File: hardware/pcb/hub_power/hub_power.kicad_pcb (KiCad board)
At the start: 2 copper layers, 44 x 81.2 mm, 58 parts, among them J1 XIAO D0-D6, J10 BAT (JST-PH), J13 USB-C, J14 XIAO PWR, J2 OLED, J4 SPK IN, J5 SPK OUT, J6 REED+BTN2, K31 G6S-2F DC5, Q1 MMUN2133LT1G, Q31 SS8050, SW1 MST-12D18G3, U1 TPS61090RSAR, U2 MCP73871-2CCI/ML, U3 INA226AIDGSR, U4 AS5600-ASOM

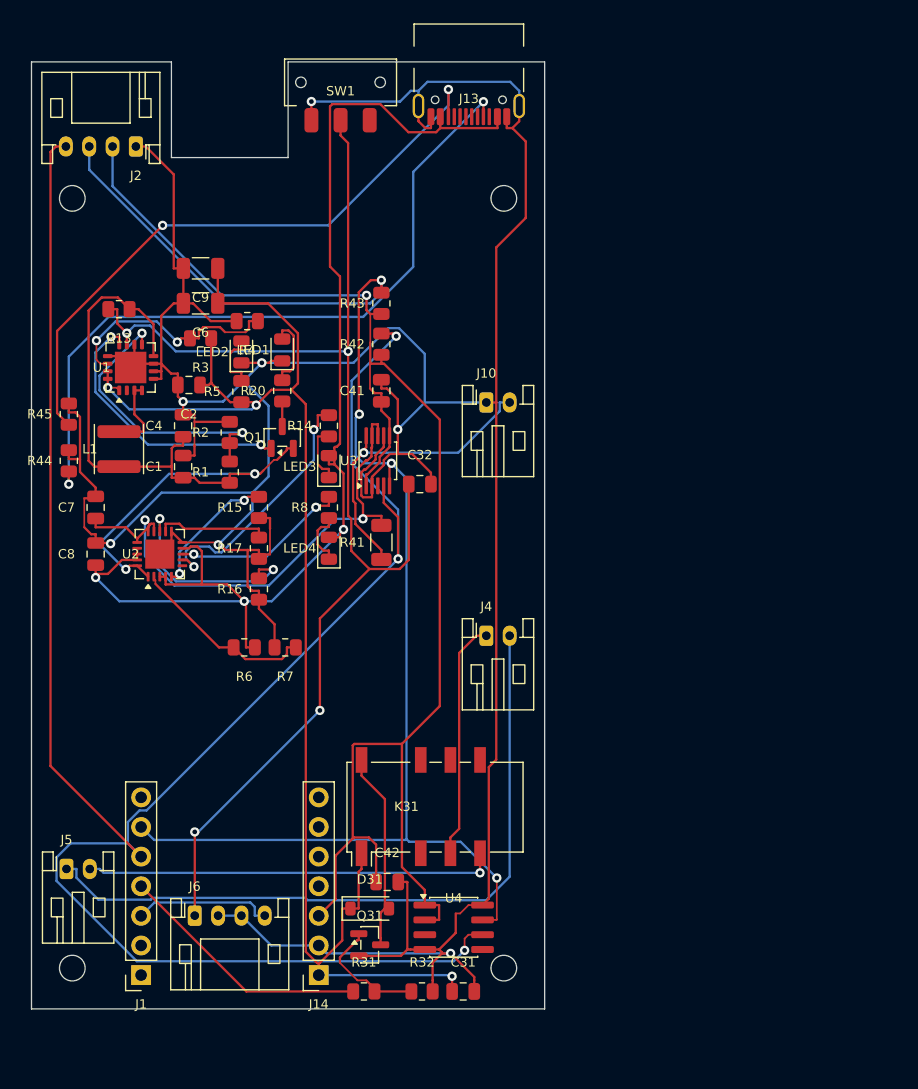
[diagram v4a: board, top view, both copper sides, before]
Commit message: リレーを立入禁止の円から出して AS5600 から離す（機構担当の B1）
- K31 の芯を Y 17.35 → 18.85。立入禁止 φ10.2（芯 36.2, 7）への食い込み 0.10 が
  余裕 1.40 になり、枠は Y 13.50〜24.20（電池の影の縁 25 まで残り 0.8）
- ついでに AS5600 の芯から 10.5 → 11.95mm 離した（リレーのコイルの磁気の件）
- B2（ブラケットの彫り込み）と B3（SOIC-8 の向き）は板側の変更なし。
  B3 は機構側のモデルが 90 度回っていたので、ランドは直さない

配線 638 本・未配線 0・DRC エラー 0・プラグの通り道 5 口すべて空き・
check_pcb は下限 0.15mm に対していちばん近いのが 0.151mm
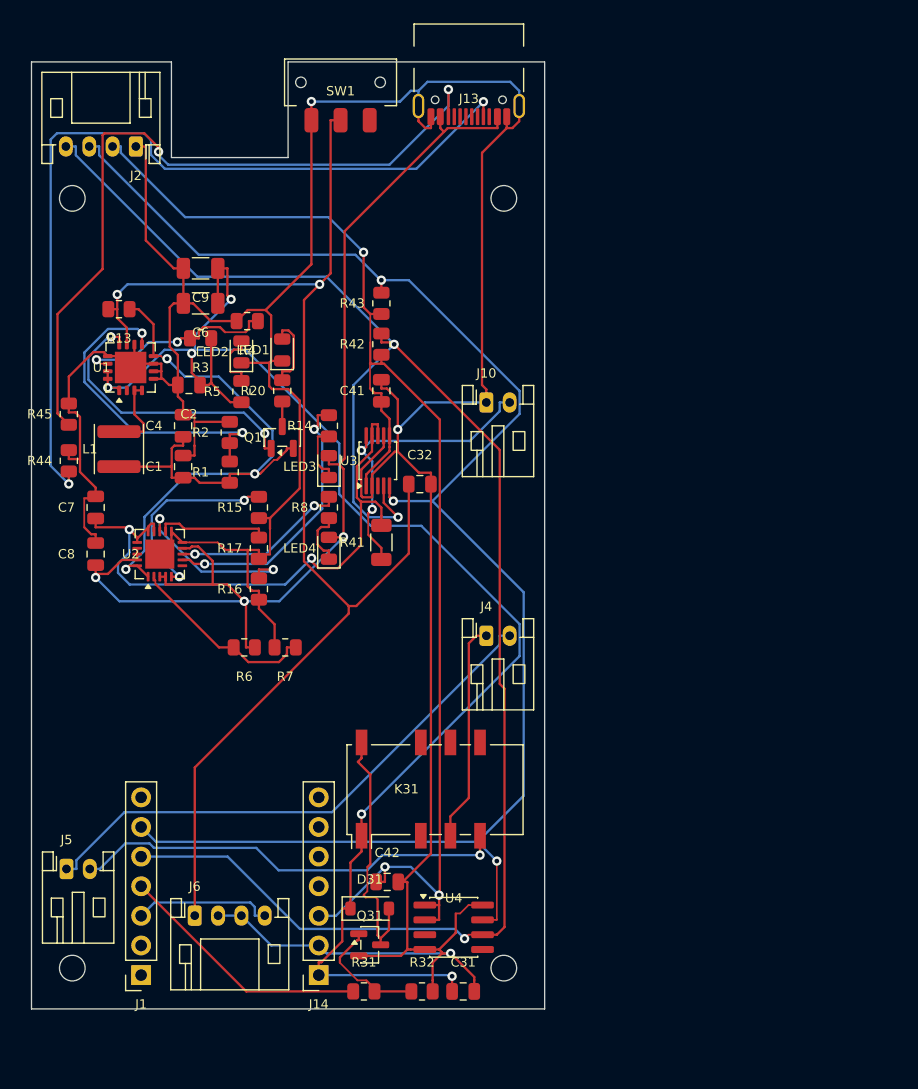
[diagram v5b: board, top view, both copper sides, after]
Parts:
- moved K31 1.50 mm to (94.7, 102.3)
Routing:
- net SDA: track 181.1 -> 148.4 mm
- net GND: track 339.6 -> 318.1 mm, vias 7 -> 3
- net SPKM: track 61.2 -> 47.2 mm
- net V33: track 130.2 -> 117.9 mm, vias 1 -> 3
- net CC1: track 62.7 -> 74.3 mm
- net SCL: track 126.1 -> 136.5 mm, vias 4 -> 3
- net CC2: track 53.7 -> 63.9 mm
- net VBUS: track 106.5 -> 97.6 mm
- net VSYS: track 67.8 -> 62.3 mm, vias 2 -> 3
- net THERM: track 11.4 -> 16.8 mm
- net VLIPO: track 46.6 -> 51.7 mm
- net COL: track 17.2 -> 22.1 mm
- net V5: track 121.0 -> 125.9 mm, vias 3 -> 5
- net LBI: track 24.6 -> 28.3 mm
- net EN: track 110.1 -> 113.1 mm, vias 4 -> 2
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
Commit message: 両面に GND のベタを敷いて板を通す・ナットと通り道の検査を足す
筐体側から「取付穴のナット（二面幅 4.0・背 1.6）の下に部品が寄っていないか」と聞かれて
数えたら 3 つ当たっていた。直す過程で自動配線が詰まったので、構造から直した。

- 🔴 ナットの検査を足した。MOUNT_KEEP は銅の話で部品の背の話ではない。
  J5 と C31 を逃がした。U4（AS5600）だけは磁石の真下から動かせないので残っている
- 🔴 プラグの通り道も「押し出す所」に入れた。入れないと他の部品が後から流れ込む
  （電源ブロックを広げたら J2 の通り道に U1 と R13 が入った）
- 🔴 CC の引き下げ 2 本を USB-C の足元へ。旧電源板の並びを写したままで 40mm 離れ、
  CC2 が 1 本つながっていなかった
- 電源ブロックを電池の影いっぱいに広げた（旧 40 × 32 の詰め方のままだった）
- 🔴 表と裏に GND のベタを敷き、島を縫うビアを 173 個打つ route.py の stitch() を足した。
  ⚠ GND は自動配線にも渡す。ベタ任せにすると U3 の細ピッチの GND にベタが入らない
- パッドはベタ直結（thermal relief を使わない）。足付きだけ thermal にすると PH や
  USB-C のシェルの幅 1.0mm のパッドで spoke が 1 本しか立たず starved_thermal が残る。
  ⚠ 代償として手はんだの GND 7 点に熱が逃げる
- drc に --refill-zones を足した（--save-board は付けない。板を KiCad に書き直させると
  次の merge() が読めなくなる）

結果: 配線 628 本 ＋ 縫うビア 173 個・**未配線 0・DRC エラー 0**・
check_sch 0 件・check_pcb は下限 0.15mm に対していちばん近いのが 0.152mm・
プラグの通り道 5 口すべて空き・パッドの位置の検算 4 点一致。

ついでに POWER.md のリードの沈み代を 0.70 → 0.58 に直した（0.30 は立った壁の値で、
平たい肉の実績は 0.42）。数は磁石の半径が決まってから数え直す。
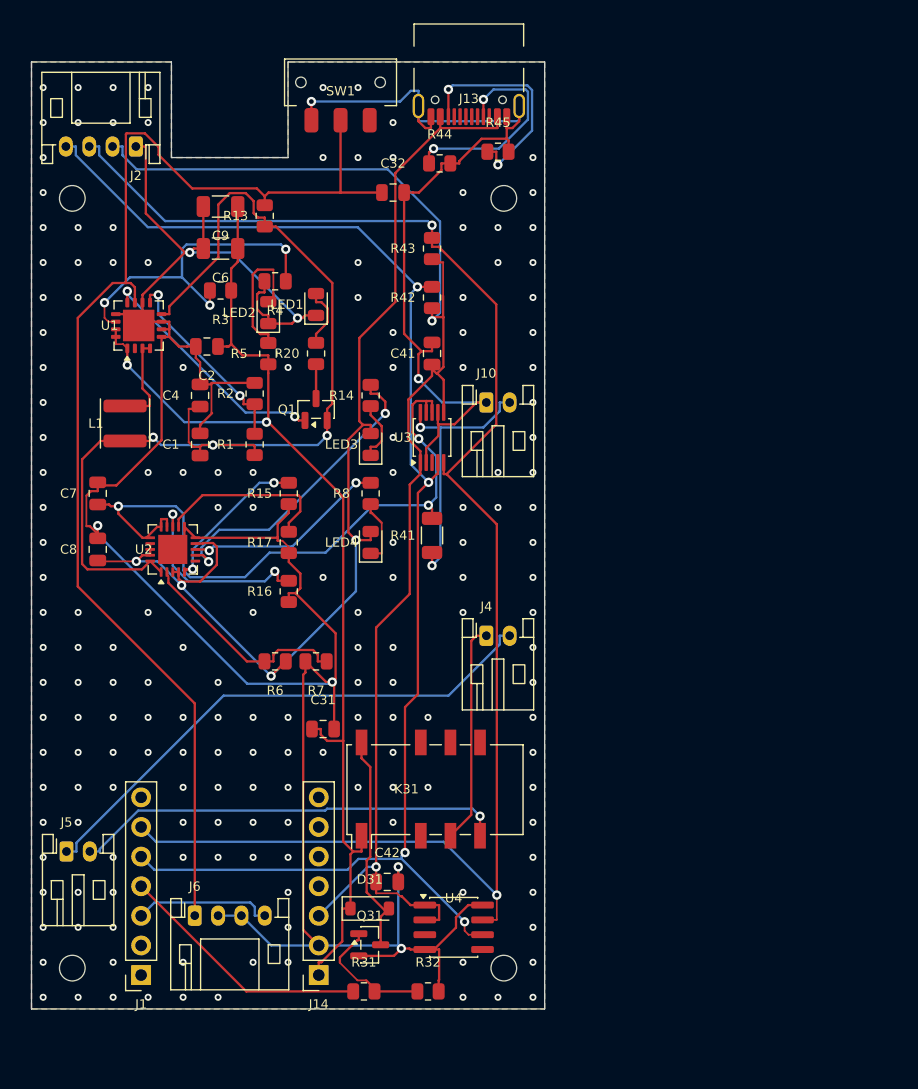
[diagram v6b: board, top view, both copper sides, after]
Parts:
- moved R45 43.1 mm to (100.0, 47.7), turned to 0 degrees
- moved R44 40.8 mm to (95.0, 48.7), turned to 0 degrees
- moved C31 25.5 mm to (85.0, 97.2)
- moved C32 25.1 mm to (91.0, 51.2)
- moved R13 14.8 mm to (80.0, 53.2), turned to 90 degrees
- moved R43 6.40 mm to (94.3, 56.0)
- moved R42 5.91 mm to (94.3, 60.2)
- moved C9 5.57 mm to (76.2, 52.4)
- moved C41 5.40 mm to (94.3, 65.0)
- moved U3 5.06 mm to (94.3, 72.2)
- moved C6 5.00 mm to (76.2, 56.0)
- moved LED1 4.86 mm to (84.4, 60.8)
- moved R3 4.44 mm to (76.2, 59.6)
- moved R14 4.42 mm to (89.1, 68.6)
- moved R41 4.39 mm to (94.3, 80.6)
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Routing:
- net CC1: track 74.3 -> 18.7 mm
- net CC2: track 63.9 -> 19.4 mm
- net V5: track 125.9 -> 98.1 mm, vias 5 -> 2
- net VSYS: track 62.3 -> 89.9 mm
- net SDA: track 148.4 -> 123.0 mm, vias 3 -> 4
- net GND: track 318.1 -> 300.4 mm, vias 3 -> 181
- net FB: track 17.4 -> 29.0 mm, vias 2 -> 3
- net LBI: track 28.3 -> 17.3 mm
- net VLIPO: track 51.7 -> 58.8 mm, vias 2 -> 3
- net N_LED2: track 5.11 -> 11.7 mm
- net PROG3: track 9.60 -> 15.4 mm
- net EN: track 113.1 -> 107.5 mm, vias 2 -> 0
- net LBO: track 24.8 -> 21.0 mm
- net THERM: track 16.8 -> 13.1 mm
- net STAT2: track 23.5 -> 26.7 mm
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- added copper zone on B.Cu, net GND
- added copper zone on F.Cu, net GND

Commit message: 背面の柱 6 本の抜きを入れて引き直す（⚠ 未配線が 1 本残っている）
🔒 調停役 2026-09-13「解放します。1 回で入れてください」。抜きは確定値で入れた。

- 外形に丸い抜きを 6 つ（OLED × 4 φ6.5・ReSpeaker × 2 φ4.0・合計 157.9mm²）。
  まわり 0.5 に銅を置かせない（0.3 だと KiCad の copper_edge_clearance が出た）
- 抜きを relax の押し出す所と DSN の keepout と縫うビアの除外に入れた
- 🔴 **OLED の柱 (3.30, 71.80) が上の縁の唯一の 4 ピンの枠を奪った。**総当たりで探したら
  PH 4 ピンが入るのは谷と右の帯（口を −X へ）の 2 つだけで、谷には J6 が居る。
  ⇒ OLED の口を右の帯（X 35〜43.6・Y 43.5〜54.5）へ回した。口は板の内側 −X を向く。
  線は伸びるが、谷へ入れた場合の 65mm より短い（芯どうし約 35mm）
- その通り道が電池の影を横切るので、電源ブロックの並びを組み替えた。
  pwr() の倍率を X 1.13 / Y 1.32 にし、通り道に落ちる 8 つ（U3・C41・R42・R8・LED3・
  R14・LED4・Q1）は手で左へ置いた
- ミュートリレーの駆動を K31 の左上の帯（Y 20〜25）へ。柱の抜きで J14 と柱のあいだが
  2.88mm しか残らなくなったため
- 🔒 取付穴 (40.5, 3.5) の U4 はナットの検査から除外した。ナットはブラケットの足の上
  （BRK_FT 2.15 ⇒ 底 6.75）で U4 の天面 6.45 を 0.30 の隙間で宙で跨ぐ

検査: 取付穴 4 か所ともナットの下は空き・プラグの通り道 5 口すべて空き・
パッドの位置の検算 4 点一致・部品の重なり 0・板からのはみ出し 0・
check_sch 0 件・check_pcb は下限 0.15mm に対していちばん近いのが 0.152mm。

🔴 **未配線が 1 本残っている**: J13（USB-C）の VBUS のパッド A4。VBUS は 4 パッドあり
3 本までつながって 1 本が届かない。原因は OLED の柱 (40.70, 71.80) の抜きが USB-C の
足元を塞いでいること。倍率を 1.08〜1.20 で振って 1.13 が最小（他は 2〜4 本）。
CC の抵抗を動かすと今度は J4 の通り道が塞がる。**次はここを解く。**
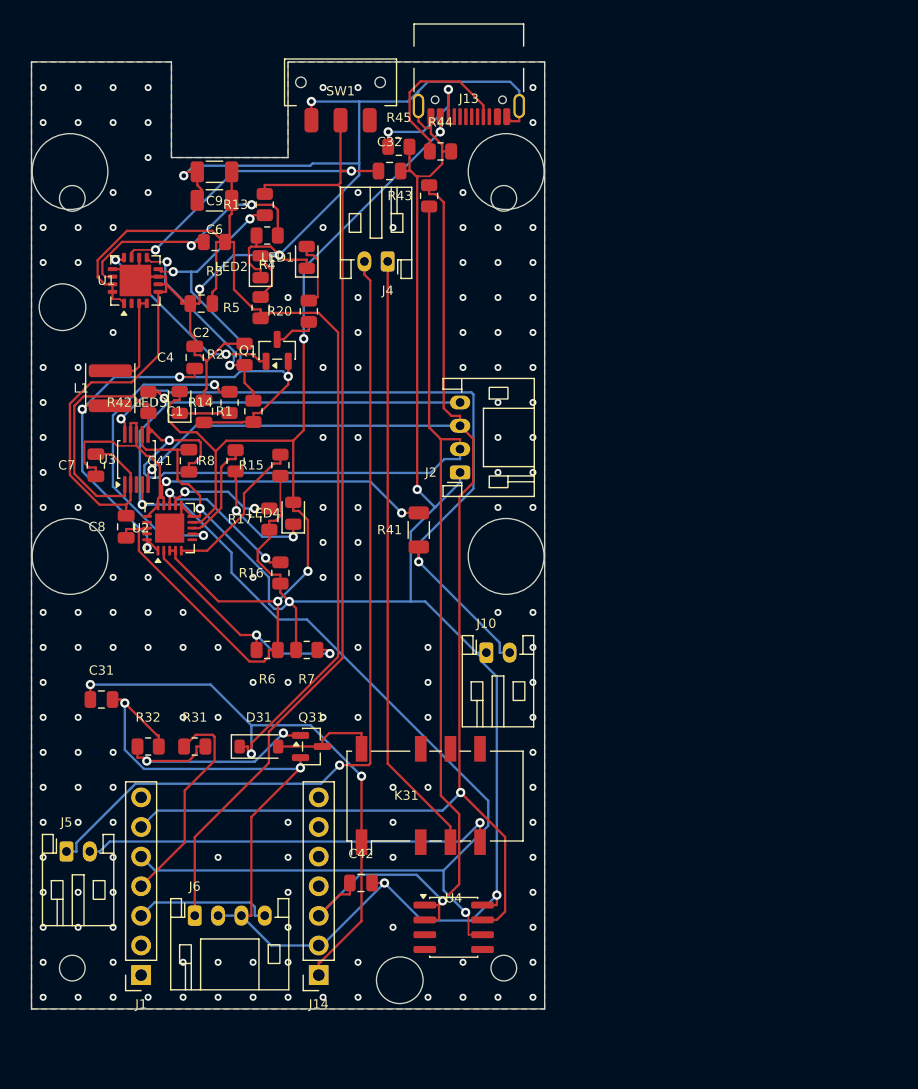
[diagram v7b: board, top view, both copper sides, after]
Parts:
- removed the C31 at (85.0, 97.2)
- removed the J10 at (99.0, 69.2)
- removed the J2 at (69.0, 47.2)
- added J4: SPK IN, Connector_JST:JST_PH_S2B-PH-K_1x02_P2.00mm_Horizontal, F.Cu at (90.5, 57.1)
- added J6: REED+BTN2, Connector_JST:JST_PH_S4B-PH-K_1x04_P2.00mm_Horizontal, F.Cu at (74.0, 113.2)
- added Q31: SS8050, Package_TO_SOT_SMD:SOT-23, F.Cu at (84.0, 98.7)
- C31: renamed from R31; value 1k -> 0.1uF; footprint Resistor_SMD:R_0805_2012Metric -> Capacitor_SMD:C_0805_2012Metric
- J10: renamed from J6; value REED+BTN2 -> BAT (JST-PH); footprint Connector_JST:JST_PH_S4B-PH-K_1x04_P2.00mm_Horizontal -> Connector_JST:JST_PH_S2B-PH-K_1x02_P2.00mm_Horizontal
- J2: renamed from J4; value SPK IN -> OLED; footprint Connector_JST:JST_PH_S2B-PH-K_1x02_P2.00mm_Horizontal -> Connector_JST:JST_PH_S4B-PH-K_1x04_P2.00mm_Horizontal
- R31: renamed from Q31; value SS8050 -> 1k; footprint Package_TO_SOT_SMD:SOT-23 -> Resistor_SMD:R_0805_2012Metric
- moved ? 75.7 mm to (63.5, 117.7)
- moved ? 75.7 mm to (100.5, 51.7)
- moved J10 33.7 mm to (99.0, 90.7)
- moved C31 33.7 mm to (66.0, 94.7)
- moved R32 31.9 mm to (70.0, 98.7)
- moved R42 25.9 mm to (70.0, 69.2)
- moved U3 25.4 mm to (69.0, 74.1)
- moved C41 22.8 mm to (73.5, 74.2)
- moved R31 22.7 mm to (74.0, 98.7)
- moved D31 16.8 mm to (79.5, 98.7)
- moved LED3 16.8 mm to (72.7, 69.2)
- moved J2 14.2 mm to (96.8, 75.2), turned to 90 degrees
- moved R14 12.1 mm to (77.0, 69.2)
- moved R8 11.9 mm to (77.5, 74.2)
- moved R45 8.51 mm to (91.5, 47.3)
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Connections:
- C31 pad 1: IN -> V5
- C31 pad 2: BASE -> GND
- J10 pad 1: EN -> GND
- J10 pad 2: GND -> BATP
- J2 pad 1: SPKP -> GND
- J2 pad 2: SPKM -> V33
- R31 pad 1: BASE -> IN
- R31 pad 2: GND -> BASE
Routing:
- net GND: track 300.4 -> 359.3 mm, vias 181 -> 168
- net BATP: track 23.5 -> 61.9 mm
- net V5: track 98.1 -> 135.3 mm, vias 2 -> 3
- net SPKP: track 18.9 -> 52.0 mm
- net V33: track 120.2 -> 147.3 mm
- net SPKM: track 46.5 -> 72.9 mm, vias 0 -> 1
- net VSYS: track 89.9 -> 72.5 mm, vias 3 -> 6
- net VLIPO: track 58.8 -> 44.6 mm, vias 3 -> 2
- net VBUS: track 96.2 -> 109.0 mm
- net BASE: track 11.0 -> 22.0 mm, vias 0 -> 2
- net COL: track 19.0 -> 9.30 mm
- net STAT1: track 17.5 -> 8.98 mm, vias 2 -> 0
- net CC2: track 19.4 -> 11.1 mm
- net N_LED2: track 11.7 -> 4.67 mm
- net SCL: track 133.7 -> 127.0 mm
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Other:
- outline, holes or cut-outs redrawn

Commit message: 板が通った — 柱の抜き 6 つ入り・未配線 0・DRC エラー 0
🔒 調停役 2026-09-13「板を動かせます」。電池（603040）と SCR_IN 0.2 が決まって
止めていた理由が消えたので、抜きを入れたまま最後まで引いた。

- 🔴 USB-C の VBUS が 1 本つながらなかったのを、**口の足元に VBUS の小さなベタ**を
  置いて解いた。VBUS は A4・B4・A9・B9 の 4 パッドあり、真ん中の A4 が両隣の信号に
  囲まれて自動配線が届かなかった。電源はふつうこう引く
- CC の引き下げ 2 本（R44・R45）を USB-C の足元から左へ逃がした。J13 の逃げ道の
  左半分を塞いでいた（右半分は柱 (40.7, 71.8) の逃げ）
- C32（EN の跳ね止め・位置に依らない）を J4 の通り道から外した

結果:
  配線 725 本 ＋ GND を縫うビア 148 個・貫通穴 71 個
  未配線 0 ／ DRC エラー 0（警告はシルクと lib_footprint_issues だけ）
  check_sch 0 件 ／ check_pcb は下限 0.15mm に対していちばん近いのが 0.151mm
  プラグの通り道 5 口すべて空き ／ 取付穴 4 か所ともナットの下は空き
  パッドの位置の検算 4 点一致 ／ 部品の重なり 0 ／ 板からのはみ出し 0
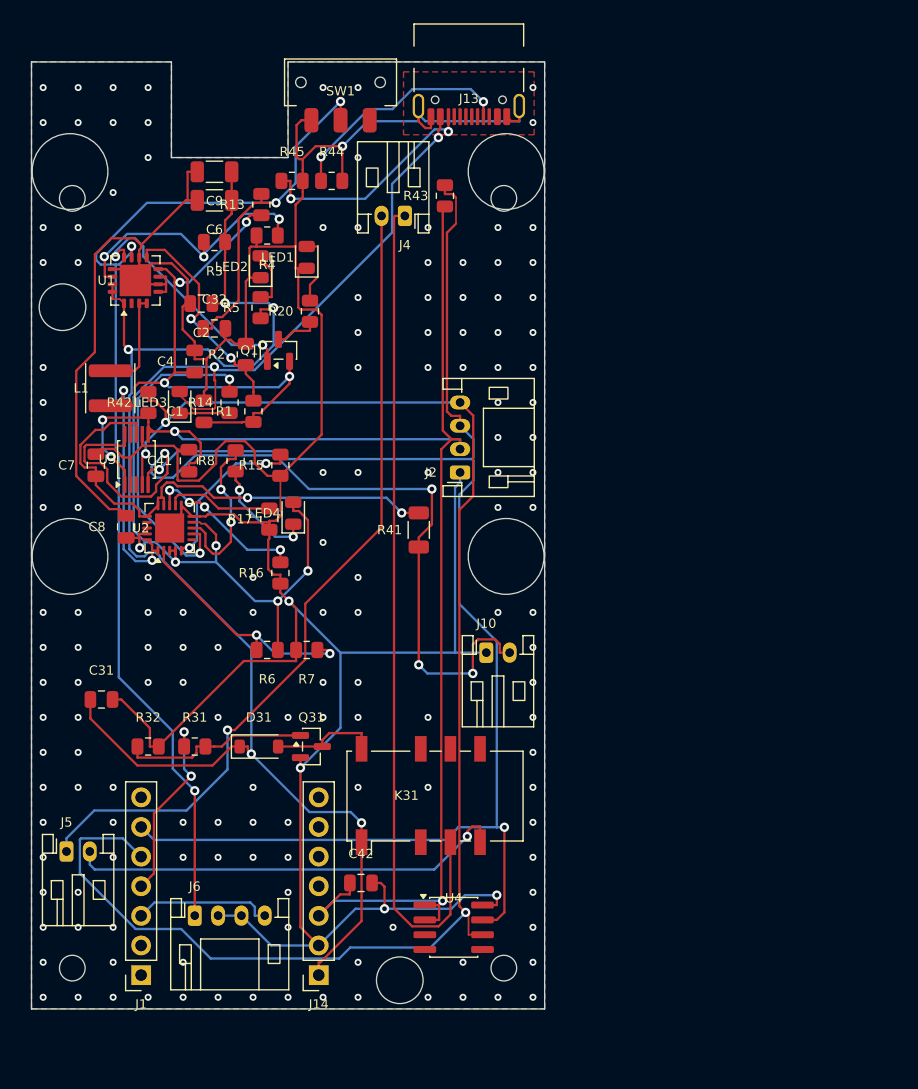
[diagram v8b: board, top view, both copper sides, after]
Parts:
- moved C32 20.2 mm to (75.7, 62.9)
- moved R44 9.67 mm to (85.7, 50.2)
- moved R45 9.61 mm to (82.3, 50.2)
- moved J4 4.17 mm to (92.0, 53.2)
- moved R43 1.36 mm to (95.4, 51.5)
- moved C4 0.34 mm to (74.0, 65.7)
- moved R13 0.29 mm to (79.7, 52.2)
- moved Q1 0.11 mm to (81.2, 64.7)
- moved R2 0.11 mm to (78.4, 65.1)
- moved R20 0.10 mm to (83.9, 61.4)
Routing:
- net GND: track 359.3 -> 327.5 mm, vias 168 -> 153
- net SPKP: track 52.0 -> 72.4 mm
- net V33: track 147.3 -> 127.5 mm, vias 2 -> 4
- net BATP: track 61.9 -> 73.3 mm, vias 2 -> 4
- net VBUS: track 109.0 -> 99.1 mm, vias 4 -> 7
- net SDA: track 121.5 -> 130.4 mm
- net CC2: track 11.1 -> 19.6 mm
- net V5: track 135.3 -> 127.8 mm, vias 3 -> 5
- net BASE: track 22.0 -> 16.1 mm, vias 2 -> 0
- net CC1: track 14.3 -> 20.1 mm, vias 0 -> 2
- net STAT1: track 8.98 -> 14.4 mm, vias 0 -> 2
- net LBO: track 17.3 -> 21.1 mm
- net EN: track 106.2 -> 110.0 mm, vias 2 -> 4
- net SCL: track 127.0 -> 130.7 mm
- net SPKM: track 72.9 -> 70.7 mm
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- added copper zone on F.Cu, net VBUS
